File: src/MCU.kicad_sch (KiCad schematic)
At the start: 42 parts, among them J3 Conn_Coaxial, J4 Conn_02x05_Odd_Even, U1 ESP32-C6, U3 W25Q64JWUUIQ, Y1 40MHz

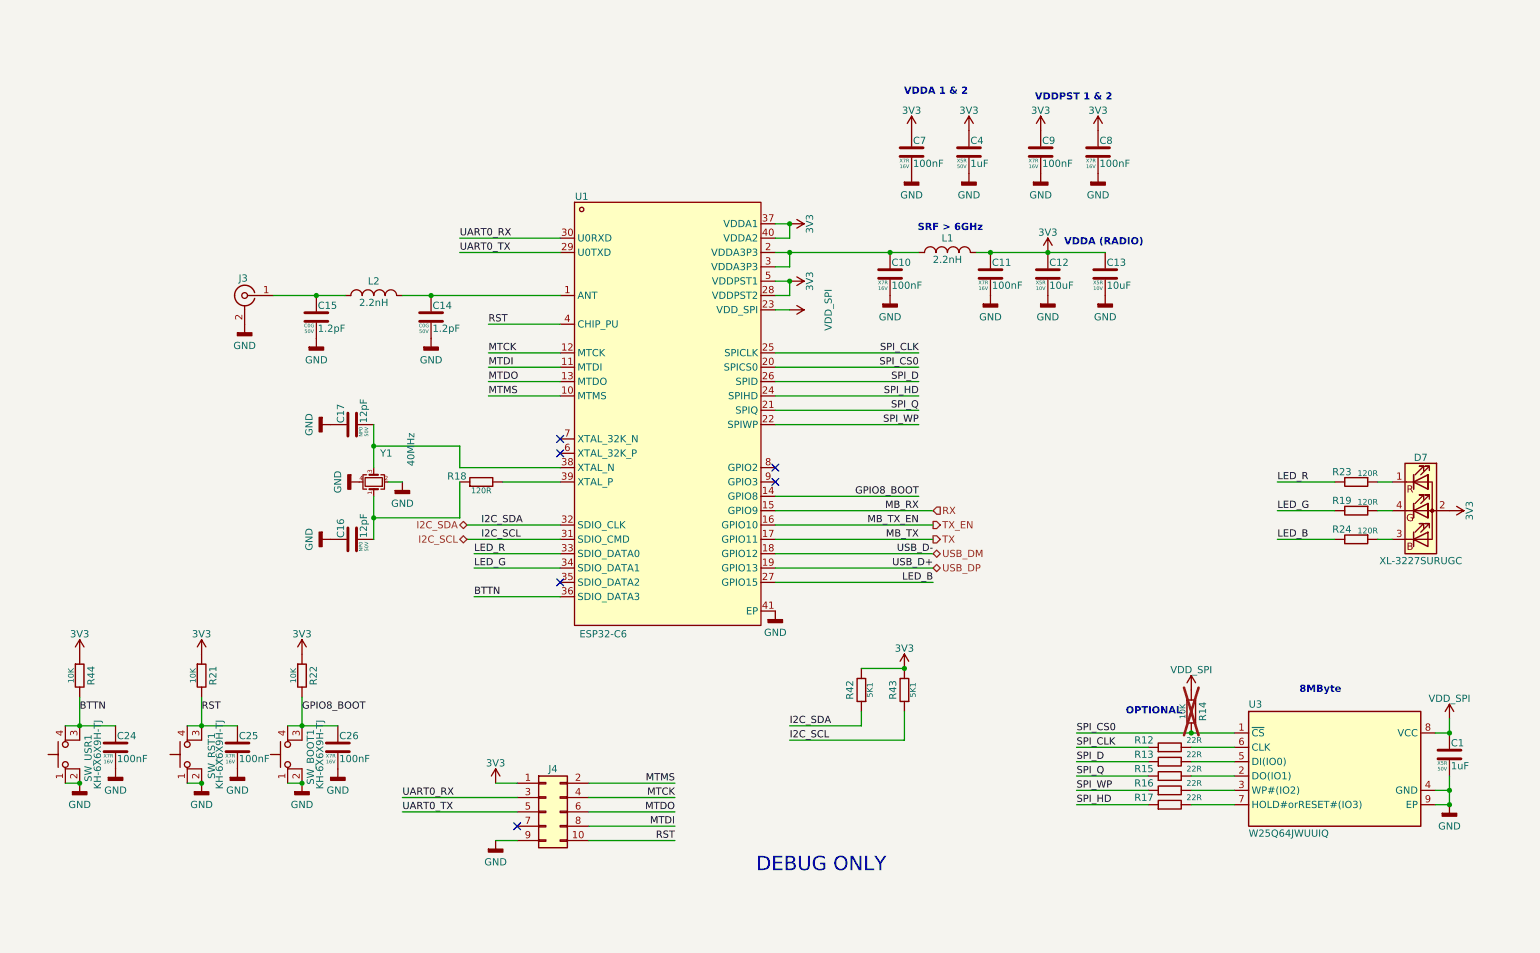
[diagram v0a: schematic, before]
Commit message: V3.1 first changes
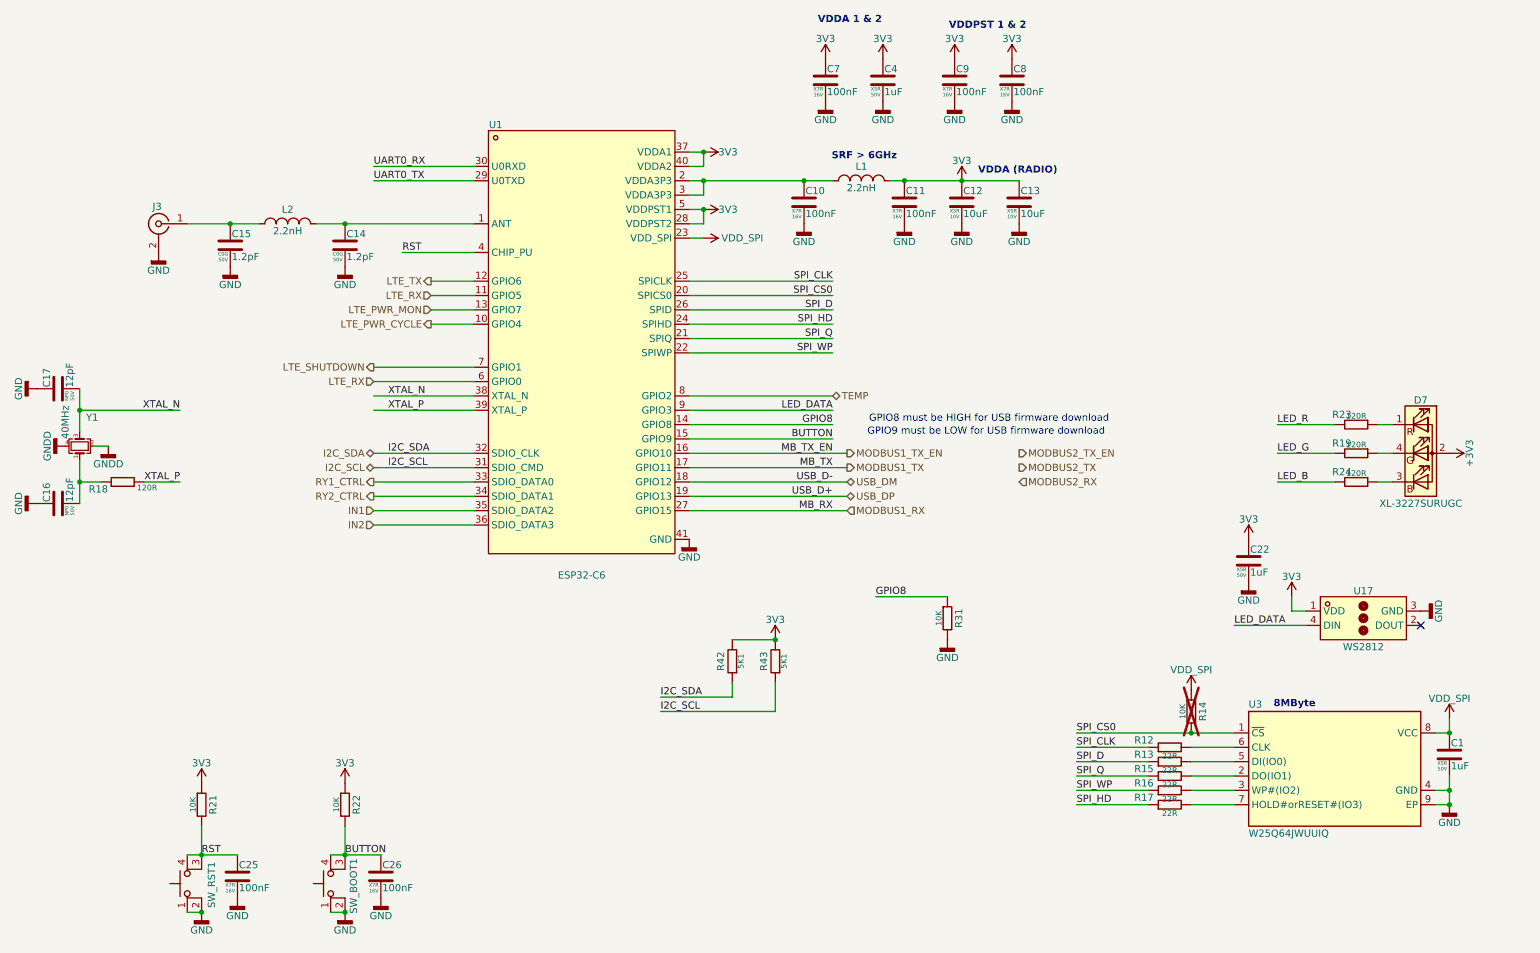
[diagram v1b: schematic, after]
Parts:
- removed C24: 100nF, 7Sigma:C_0402_1005Metric, symbol Capacitor:CL05B104KO5NNNC
- removed J4: Conn_02x05_Odd_Even, 7Sigma:IDC-SMD_10P-P1.27-3220-10-0300-00, symbol Connectors:HX JN1.27-2x5 TP H4.9
- removed R44: 10K, 7Sigma:R_0402_1005Metric, symbol Resistor:0402WGF1002TCE
- removed SW_USR1: KH-6X6X9H-TJ, 7Sigma:SW-TH_4P-L6.0-W6.0-P4.50-LS6.5-H9.0, symbol Buttons:KH-6X6X9H-TJ
- added C22: 1uF, 7Sigma:C_0402_1005Metric, symbol Capacitor:GRM155R61H105KE05D
- added R31: 10K, 7Sigma:R_0402_1005Metric, symbol Resistor:0402WGF1002TCE
- added U17: WS2812, 7Sigma:LED-SMD_4P-L1.3-W1.3-P0.80_WS2812E-1313, symbol ICs:WS2812E-1313
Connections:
- net MTDI is gone; now on net LTE_RX: U1.11 (MTDI)
- net RX is gone; now on net BUTTON: U1.15 (GPIO9)
- net 3V3: now also C22.1, U17.1 (VDD); no longer D7.2 (A)
- net GND: now also C22.2, R31.2, U17.3 (GND); no longer Y1.2, Y1.4
- net LED_B: no longer U1.27 (GPIO15)
- net LED_G: no longer U1.34 (SDIO_DATA1)
- net LED_R: no longer U1.33 (SDIO_DATA0)
- net XTAL_N: now reaches C17.2, U1.38 (XTAL_N), Y1.3
- net IN1: now reaches U1.35 (SDIO_DATA2)
- net XTAL_P: now reaches R18.2, U1.39 (XTAL_P)
- net LTE_RX: now reaches U1.6 (GPIO0)
- net LTE_SHUTDOWN: now reaches U1.7 (GPIO1)
- net TEMP: now reaches U1.8 (GPIO2)
- net LED_DATA: now reaches U1.9 (GPIO3)
- net LED_DATA: now also U17.4 (DIN)
- net BTTN renamed IN2
- net GPIO8_BOOT renamed BUTTON
- net BUTTON: no longer U1.14 (GPIO8)
- net MTCK renamed LTE_TX
- net MTDO renamed LTE_PWR_MON
- net MTMS renamed LTE_PWR_CYCLE
- net TX renamed MODBUS1_TX
- net TX_EN renamed MODBUS1_TX_EN
- new net +3V3: D7.2 (A)
- new net GNDD: Y1.2, Y1.4
- new net GPIO8: R31.1, U1.14 (GPIO8)
- new net MODBUS1_RX: U1.27 (GPIO15)
- new net RY1_CTRL: U1.33 (SDIO_DATA0)
- new net RY2_CTRL: U1.34 (SDIO_DATA1)
- no-connect marks 6 -> 1
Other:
- note added: "GPIO8 must be HIGH for USB firmware download"
- note added: "GPIO9 must be LOW for USB firmware download"
- note removed: "DEBUG ONLY"
- note removed: "OPTIONAL"
- moved on the sheet: C10, C11, C12, C13, C14, C15, C16, C17, C25, C26, C4, C7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

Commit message: ongoing work
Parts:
- removed D7: XL-3227SURUGC, 7Sigma:LED-SMD_4P-L1.6-W1.5-BR, symbol LEDs:XL-1615RGBC-RF
- removed J3: Conn_Coaxial, 7Sigma:SMA-SMD_BWSMA-KE-P001, symbol Connectors:BWSMA-KE-P001
- removed R19, R23, R24: 120R, 7Sigma:R_0402_1005Metric, symbol Resistor:0402WGF1200TCE
- removed SW_BOOT1, SW_RST1: KH-6X6X9H-TJ, 7Sigma:SW-TH_4P-L6.0-W6.0-P4.50-LS6.5-H9.0, symbol Buttons:KH-6X6X9H-TJ
- added J5: Conn_Coaxial, 7Sigma:SMA-SMD_BWSMA-KE-P001, symbol Connectors:BWSMA-KE-P001
- added LP1: FIX-LEMB2-4.8V0-F, 7Sigma:FIX-LEMB2-4.8V0-F, symbol Mechanical_7S:FIX-LEMB2-4.8V0-F
- added SW1: TC-6615-9.0-160G, 7Sigma:SW-TH_4P-RA-L6.0-W6.0-H9.0, symbol Buttons:TC-6615-9.0-160G
- added SW2: KH-6X6X7H-STM, 7Sigma:SW-SMD_4P-L6.0-W6.0-P4.50-LS9.0-H7.0, symbol Buttons:KH-6X6X7H-STM
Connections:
- net GNDD is gone; now on net GND: Y1.2, Y1.4
- net BUTTON: now also SW2.3 (K), SW2.4 (A)
- net GND: now also J5.2 (Ext), SW1.1, SW1.2, SW2.1, SW2.2
- net LTE_RX: no longer U1.6 (GPIO0)
- net RST: now also SW1.3 (K), SW1.4 (A)
- net at C15.1, L2.1: now also J5.1 (In)
- net IN1: no longer names the net of U1.35 (SDIO_DATA2)
- net IN2: no longer names the net of U1.36 (SDIO_DATA3)
- no-connect marks 1 -> 0

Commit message: Layout progress
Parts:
- removed SW1: TC-6615-9.0-160G, 7Sigma:SW-TH_4P-RA-L6.0-W6.0-H9.0, symbol Buttons:TC-6615-9.0-160G
- added C46, C47: 100nF, 7Sigma:C_0402_1005Metric, symbol Capacitor:CL05B104KO5NNNC
- added LP2, LP3: FIX-LEMB2-4.8V0-F, 7Sigma:FIX-LEMB2-4.8V0-F, symbol Mechanical_7S:FIX-LEMB2-4.8V0-F
- added SW1: KH-6X6X4.3H-STM, 7Sigma:SW-SMD_4P-L6.0-W6.0-P4.50-LS9.0-H4.3, symbol Buttons:KH-6X6X4.3H-STM
- added U18, U20: WS2812, 7Sigma:LED-SMD_4P-L1.3-W1.3-P0.80_WS2812E-1313, symbol ICs:WS2812E-1313
- C1, C4: Price @1 USD (none) -> 0.0308; Price @100 USD (none) -> 0.0308; Price @Bulk USD (none) -> 0.0209; Price Bulk Qty (none) -> 600; Price Source (none) -> LCSC; Price Updated (none) -> 2026-05-14
- C10, C11, C25, C26, C7, C8, C9: Price @1 USD (none) -> 0.0015; Price @100 USD (none) -> 0.0015; Price @Bulk USD (none) -> 0.0012; Price Bulk Qty (none) -> 1000; Price Source (none) -> LCSC; Price Updated (none) -> 2026-05-14
- C12, C13: Price @1 USD (none) -> 0.0090; Price @100 USD (none) -> 0.0090; Price @Bulk USD (none) -> 0.0064; Price Bulk Qty (none) -> 600; Price Source (none) -> LCSC; Price Updated (none) -> 2026-05-14
- C14, C15: Price @1 USD (none) -> 0.0238; Price @100 USD (none) -> 0.0238; Price @Bulk USD (none) -> 0.0190; Price Bulk Qty (none) -> 500; Price Source (none) -> LCSC; Price Updated (none) -> 2026-05-14
- C16, C17: Price @1 USD (none) -> 0.0012; Price @100 USD (none) -> 0.0012; Price @Bulk USD (none) -> 0.0009; Price Bulk Qty (none) -> 1000; Price Source (none) -> LCSC; Price Updated (none) -> 2026-05-14
- C22: value 1uF -> 100nF; symbol Capacitor:GRM155R61H105KE05D -> Capacitor:CL05B104KO5NNNC; Dielectric X5R -> X7R; JLCPCB Part Class (none) -> Basic Part; LCSC Part C1518208 -> C1525; Manufacturer 1 Murata Electronics -> Samsung Electro-Mechanics; Manufacturer Part Number 1 GRM155R61H105KE05D -> CL05B104KO5NNNC; Price @1 USD (none) -> 0.0015; Price @100 USD (none) -> 0.0015; Price @Bulk USD (none) -> 0.0012; Price Bulk Qty (none) -> 1000; Price Source (none) -> LCSC; Price Updated (none) -> 2026-05-14; Supplier Part Number 1 C1518208 -> C1525; Tolerance 1% -> 10%; Voltage 50V -> 16V
- J5: Price @1 USD (none) -> 0.3843; Price @100 USD (none) -> 0.2076; Price @Bulk USD (none) -> 0.1897; Price Bulk Qty (none) -> 1000; Price Source (none) -> LCSC; Price Updated (none) -> 2026-05-14
- L1, L2: Price @1 USD (none) -> 0.0490; Price @100 USD (none) -> 0.0402; Price @Bulk USD (none) -> 0.0324; Price Bulk Qty (none) -> 1000; Price Source (none) -> LCSC; Price Updated (none) -> 2026-05-14
- LP1: Manufacturer FIX&fasten -> (none); Manufacturer 1 (none) -> FIX&fasten; Manufacturer Part Number FIX-LEMB2-4.8V0-F -> (none); Manufacturer Part Number 1 (none) -> FIX-LEMB2-4.8V0-F; Price @Bulk USD (none) -> 0.0720; Price Bulk Qty (none) -> 1000; Price Source (none) -> Manual
- R12, R13, R15, R16, R17: Price @1 USD (none) -> 0.0007; Price @100 USD (none) -> 0.0007; Price @Bulk USD (none) -> 0.0006; Price Bulk Qty (none) -> 1000; Price Source (none) -> LCSC; Price Updated (none) -> 2026-05-14
- R14, R21, R22, R31: Price @1 USD (none) -> 0.0013; Price @100 USD (none) -> 0.0013; Price @Bulk USD (none) -> 0.0011; Price Bulk Qty (none) -> 1000; Price Source (none) -> LCSC; Price Updated (none) -> 2026-05-14
- R18: Price @1 USD (none) -> 0.0011; Price @100 USD (none) -> 0.0011; Price @Bulk USD (none) -> 0.0009; Price Bulk Qty (none) -> 1000; Price Source (none) -> LCSC; Price Updated (none) -> 2026-05-14
- R42, R43: Price @1 USD (none) -> 0.0009; Price @100 USD (none) -> 0.0009; Price @Bulk USD (none) -> 0.0007; Price Bulk Qty (none) -> 1000; Price Source (none) -> LCSC; Price Updated (none) -> 2026-05-14
- SW2: Price @1 USD (none) -> 0.0260; Price @100 USD (none) -> 0.0260; Price @Bulk USD (none) -> 0.0161; Price Bulk Qty (none) -> 800; Price Source (none) -> LCSC; Price Updated (none) -> 2026-05-14
- U1: Price @1 USD (none) -> 2.7877; Price @100 USD (none) -> 2.1605; Price @Bulk USD (none) -> 2.0154; Price Bulk Qty (none) -> 1000; Price Source (none) -> LCSC; Price Updated (none) -> 2026-05-14
- U17: Price @1 USD (none) -> 0.0817; Price @100 USD (none) -> 0.0639; Price @Bulk USD (none) -> 0.0484; Price Bulk Qty (none) -> 1000; Price Source (none) -> LCSC; Price Updated (none) -> 2026-05-14
- U3: value W25Q64JWUUIQ -> W25Q64JVSSIQ; footprint 7Sigma:Winbond_USON-8-2EP_3x4mm_P0.8mm_EP0.2x0.8mm -> 7Sigma:SOIC-8_5.3x5.3mm_P1.27mm; symbol ICs:W25Q64JWUUIQ -> ICs:W25Q64JVSSIQ; LCSC Part C6604692 -> C179171; Manufacturer 1 Winbond -> Winbond Elec; Manufacturer Part Number 1 W25Q64JWUUIQ -> W25Q64JVSSIQ; Price @1 USD (none) -> 1.6443; Price @100 USD (none) -> 1.1886; Price @Bulk USD (none) -> 1.1156; Price Bulk Qty (none) -> 1000; Price Source (none) -> LCSC; Price Updated (none) -> 2026-05-14; Supplier Part Number 1 C6604692 -> C179171
- Y1: Price @1 USD (none) -> 0.0841; Price @100 USD (none) -> 0.0681; Price @Bulk USD (none) -> 0.0541; Price Bulk Qty (none) -> 500; Price Source (none) -> LCSC; Price Updated (none) -> 2026-05-14
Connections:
- net 3V3: now also C46.1, C47.1, U18.1 (VDD), U20.1 (VDD)
- net GND: now also C46.2, C47.2, SW1.1, SW1.2, U18.3 (GND), U20.3 (GND); no longer U3.9 (EP)
- net MODBUS1_RX: now also U1.36 (SDIO_DATA3); no longer U1.27 (GPIO15)
- net MODBUS1_TX: now also U1.34 (SDIO_DATA1); no longer U1.17 (GPIO11)
- net MODBUS1_TX_EN: now also U1.35 (SDIO_DATA2); no longer U1.16 (GPIO10)
- net RST: now also SW1.3 (K), SW1.4 (A)
- net RY1_CTRL: now also U1.27 (GPIO15); no longer U1.33 (SDIO_DATA0)
- net RY2_CTRL: now also U1.16 (GPIO10); no longer U1.34 (SDIO_DATA1)
- net at U17.2 (DOUT): now also U18.4 (DIN)
- new net: U18.2 (DOUT), U20.4 (DIN)
- no-connect marks 0 -> 4
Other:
- moved on the sheet: C22, LP1, U17

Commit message: floorplan changed, check in
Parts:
- SW1: value KH-6X6X4.3H-STM -> TS24CA; footprint 7Sigma:SW-SMD_4P-L6.0-W6.0-P4.50-LS9.0-H4.3 -> 7Sigma:SW-SMD_TS24CA; symbol Buttons:KH-6X6X4.3H-STM -> Buttons:TS24CA; LCSC Part C2837530 -> C393942; Manufacturer 1 Shenzhen Kinghelm Elec -> SHOU HAN; Manufacturer Part Number 1 KH-6X6X4.3H-STM -> TS24CA; Price @1 USD 0.0206 -> 0.0252; Price @100 USD 0.0206 -> 0.0252; Price @Bulk USD 0.0164 -> 0.0171; Price Bulk Qty 500 -> 600; Supplier Part Number 1 C2837530 -> C393942
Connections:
- net GND: no longer SW1.2
- net RST: now also SW1.2; no longer SW1.3 (K), SW1.4 (A)
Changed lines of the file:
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@@
 	)
 	(symbol
-		(lib_id "Buttons:KH-6X6X4.3H-STM")
+		(lib_id "Buttons:TS24CA")
 		(at 50.8 170.18 90)
 		(unit 1)
@@
 			)
 		)
-		(property "Value" "KH-6X6X4.3H-STM"
-			(at 53.975 170.18 0)
-			(show_name no)
-			(do_not_autoplace no)
-			(effects
-				(font
-					(size 1.27 1.27)
-				)
-			)
-		)
-		(property "Footprint" "7Sigma:SW-SMD_4P-L6.0-W6.0-P4.50-LS9.0-H4.3"
-			(at 43.18 170.18 0)
+		(property "Value" "TS24CA"
+			(at 52.324 170.18 0)
 			(hide yes)
 			(show_name no)
@@
 			)
 		)
-		(property "Datasheet" "https://wmsc.lcsc.com/wmsc/upload/file/pdf/v2/lcsc/2212051012_Shenzhen-Kinghelm-Elec-KH-6X6X4-3H-STM_C2837530.pdf"
-			(at 43.18 170.18 0)
+		(property "Footprint" "7Sigma:SW-SMD_TS24CA"
+			(at 45.72 170.18 0)
 			(hide yes)
 			(show_name no)
@@
 			)
 		)
-		(property "Description" "SMD Tactile Switch 6.0x6.0mm Top Actuation Height 4.3mm"
+		(property "Datasheet" "https://wmsc.lcsc.com/wmsc/upload/file/pdf/v2/lcsc/2404241539_SHOU-HAN-TS24CA_C393942.pdf"
+			(at 45.72 170.18 0)
+			(hide yes)
+			(show_name no)
+			(do_not_autoplace no)
+			(effects
+				(font
+					(size 1.27 1.27)
+				)
+			)
+		)
+		(property "Description" "SMD Tactile Switch 2.5x2.5mm Top Actuation Height 0.55mm"
 			(at 50.8 170.18 0)
 			(hide yes)
@@
 			)
 		)
-		(property "Manufacturer 1" "Shenzhen Kinghelm Elec"
+		(property "Manufacturer 1" "SHOU HAN"
 			(at 50.8 170.18 0)
 			(hide yes)
@@
 			)
 		)
-		(property "Manufacturer Part Number 1" "KH-6X6X4.3H-STM"
+		(property "Manufacturer Part Number 1" "TS24CA"
 			(at 50.8 170.18 0)
 			(hide yes)
@@
 			)
 		)
-		(property "Supplier Part Number 1" "C2837530"
+		(property "Supplier Part Number 1" "C393942"
 			(at 50.8 170.18 0)
 			(hide yes)
@@
 			)
 		)
-		(property "LCSC Part" "C2837530"
+		(property "LCSC Part" "C393942"
 			(at 50.8 170.18 0)
 			(hide yes)
@@
 			)
 		)
-		(property "Price @1 USD" "0.0206"
+		(property "Price @1 USD" "0.0252"
 			(at 50.8 170.18 0)
 			(hide yes)
@@
 			)
 		)
-		(property "Price @100 USD" "0.0206"
+		(property "Price @100 USD" "0.0252"
 			(at 50.8 170.18 0)
 			(hide yes)
@@
 			)
 		)
-		(property "Price @Bulk USD" "0.0164"
+		(property "Price @Bulk USD" "0.0171"
 			(at 50.8 170.18 0)
 			(hide yes)
@@
 			)
 		)
-		(property "Price Bulk Qty" "500"
+		(property "Price Bulk Qty" "600"
 			(at 50.8 170.18 0)
 			(hide yes)
@@
 			)
 		)
-		(property "Manufacturer" ""
-			(at 50.8 170.18 0)
-			(hide yes)
-			(show_name no)
-			(do_not_autoplace no)
-			(effects
-				(font
-					(size 1.27 1.27)
-				)
-			)
-		)
-		(property "Manufacturer Part Number" ""
-			(at 50.8 170.18 0)
-			(hide yes)
-			(show_name no)
-			(do_not_autoplace no)
-			(effects
-				(font
-					(size 1.27 1.27)
-				)
-			)
-		)
-		(property "on_board" ""
-			(at 50.8 170.18 0)
-			(hide yes)
-			(show_name no)
-			(do_not_autoplace no)
-			(effects
-				(font
-					(size 1.27 1.27)
-				)
-			)
-		)
-		(pin "3"
-		)
 		(pin "1"
 		)
 		(pin "2"
 		)
-		(pin "4"
-		)
 		(instances

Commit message: PCB layout continued
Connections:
- net I2C_SCL: now also U1.12 (MTCK); no longer U1.31 (SDIO_CMD)
- net I2C_SDA: now also U1.11 (MTDI); no longer U1.32 (SDIO_CLK)
- net LED_DATA: now also U1.32 (SDIO_CLK); no longer U1.9 (GPIO3)
- net LTE_PWR_CYCLE: now also U1.31 (SDIO_CMD); no longer U1.10 (MTMS)
- net LTE_PWR_MON: now also U1.7 (GPIO1); no longer U1.13 (MTDO)
- net LTE_RX: now also U1.9 (GPIO3); no longer U1.11 (MTDI)
- net LTE_SHUTDOWN: now also U1.17 (GPIO11); no longer U1.7 (GPIO1)
- net LTE_TX: now also U1.8 (GPIO2); no longer U1.12 (MTCK)
- net RY1_CTRL: now also U1.13 (MTDO); no longer U1.27 (GPIO15)
- net TEMP: now also U1.10 (MTMS); no longer U1.8 (GPIO2)
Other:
- moved on the sheet: C14, C15, J5, L2
